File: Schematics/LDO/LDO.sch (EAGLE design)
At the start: 58 parts, among them IC1 LM317MBSTT3, IC2 LM317MBSTT3, Q1 32.768kHz, X1 MINI-USB-SHIELD-UX60-MB-5ST, X2 RJ45

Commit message: Layout Update
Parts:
- removed LED2: GREEN, led:LED5MM
- removed R2: 330, rcl:R-US_R0603
- removed U$4: SPST, Switches_SPST:SPST
- added H1, H2, H3, H4: MOUNT-HOLE3.0, holes:MOUNT-HOLE3.0
- ISP: device pinhead:PINHD-2X5/90 -> con-samtec:FTSH-105-01-L-DV-K
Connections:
- removed net N$12: LED2.C, R2.2
- removed net N$22: U$1.40
- removed net N$45: U$1.8, U$4.A1, U$4.A2
- new net PE: C13.1, R10.1, X1.GND1, X1.GND2, X1.GND3, X1.GND4
- net +3V3: now also C16.2, U$1.17, U$5.B1, U$5.B2, U$6.B1, U$6.B2
- net +5V: now also X2.4; no longer C16.2, U$1.17, X2.5
- net AGND: now also C14.1, C15.1, C3.1, C6.1, U$1.47, X2.3; no longer C13.1, R10.1, U$4.B1, U$4.B2, U$5.B1, U$5.B2, U$6.B1, U$6.B2, X1.GND1, X1.GND2, X1.GND3, X1.GND4
- net ANALOGINPUT: now also X2.7; no longer X2.2
- net GND: now also X1.4; no longer C14.1, C15.1, C3.1, C6.1, R2.1, U$1.47, X2.6
- net N$18: now also X2.5; no longer X2.3
- net N$19: now also X2.6; no longer X2.4
- net N$20: now also X2.2; no longer X2.7
- net N$21: now also X2.1; no longer X2.8
- net N$41: now also U$1.15; no longer U$1.9
- net N$42: now also X2.8; no longer X2.1
- net N$44: now also U$1.16; no longer U$1.11
- net V+: no longer LED2.A
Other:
- moved on the sheet: R13, X2

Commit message: LDO Layout
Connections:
- removed net AGND: C14.1, C15.1, C3.1, C6.1, U$1.47, X2.3
- net GND: now also C14.1, C15.1, C3.1, C6.1, U$1.47, X2.3
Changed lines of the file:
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@@
 <part name="+3V12" library="supply1" deviceset="+3V3" device=""/>
 <part name="GND4" library="supply1" deviceset="GND" device=""/>
-<part name="AGND6" library="supply1" deviceset="AGND" device=""/>
-<part name="AGND7" library="supply1" deviceset="AGND" device=""/>
-<part name="AGND8" library="supply1" deviceset="AGND" device=""/>
 <part name="PE1" library="supply1" deviceset="PE" device=""/>
-<part name="AGND1" library="supply1" deviceset="AGND" device=""/>
 <part name="GND6" library="supply1" deviceset="GND" device=""/>
 <part name="GND10" library="supply1" deviceset="GND" device=""/>
@@
 <part name="H3" library="holes" deviceset="MOUNT-HOLE" device="3.0"/>
 <part name="H4" library="holes" deviceset="MOUNT-HOLE" device="3.0"/>
+<part name="GND14" library="supply1" deviceset="GND" device=""/>
+<part name="GND15" library="supply1" deviceset="GND" device=""/>
+<part name="GND16" library="supply1" deviceset="GND" device=""/>
+<part name="GND21" library="supply1" deviceset="GND" device=""/>
 </parts>
 <sheets>
@@
 <instance part="+3V12" gate="G$1" x="-17.78" y="45.72"/>
 <instance part="GND4" gate="1" x="-22.86" y="58.42"/>
-<instance part="AGND6" gate="VR1" x="35.56" y="88.9"/>
-<instance part="AGND7" gate="VR1" x="63.5" y="81.28"/>
-<instance part="AGND8" gate="VR1" x="66.04" y="73.66"/>
 <instance part="PE1" gate="M" x="127" y="-15.24"/>
-<instance part="AGND1" gate="VR1" x="-17.78" y="71.12"/>
 <instance part="GND6" gate="1" x="-38.1" y="35.56"/>
 <instance part="GND10" gate="1" x="-45.72" y="35.56"/>
@@
 <instance part="H3" gate="G$1" x="48.26" y="-27.94"/>
 <instance part="H4" gate="G$1" x="58.42" y="-27.94"/>
+<instance part="GND14" gate="1" x="-17.78" y="71.12"/>
+<instance part="GND15" gate="1" x="35.56" y="88.9"/>
+<instance part="GND16" gate="1" x="66.04" y="73.66"/>
+<instance part="GND21" gate="1" x="63.5" y="81.28"/>
 </instances>
 <busses>
@@
 <pinref part="GND13" gate="1" pin="GND"/>
 </segment>
+<segment>
+<pinref part="C15" gate="G$1" pin="1"/>
+<pinref part="GND14" gate="1" pin="GND"/>
+</segment>
+<segment>
+<pinref part="C14" gate="G$1" pin="1"/>
+<wire x1="35.56" y1="91.44" x2="33.02" y2="91.44" width="0.1524" layer="91"/>
+<pinref part="X2" gate="G$1" pin="3"/>
+<wire x1="17.78" y1="111.76" x2="17.78" y2="93.98" width="0.1524" layer="91"/>
+<wire x1="17.78" y1="93.98" x2="33.02" y2="93.98" width="0.1524" layer="91"/>
+<wire x1="33.02" y1="93.98" x2="33.02" y2="91.44" width="0.1524" layer="91"/>
+<junction x="33.02" y="91.44"/>
+<pinref part="GND15" gate="1" pin="GND"/>
+</segment>
+<segment>
+<pinref part="U$1" gate="G$1" pin="47"/>
+<wire x1="45.72" y1="78.74" x2="66.04" y2="78.74" width="0.1524" layer="91"/>
+<wire x1="66.04" y1="78.74" x2="66.04" y2="76.2" width="0.1524" layer="91"/>
+<pinref part="C3" gate="G$1" pin="1"/>
+<wire x1="66.04" y1="76.2" x2="63.5" y2="76.2" width="0.1524" layer="91"/>
+<pinref part="GND16" gate="1" pin="GND"/>
+<junction x="66.04" y="76.2"/>
+</segment>
+<segment>
+<pinref part="C6" gate="G$1" pin="1"/>
+<pinref part="GND21" gate="1" pin="GND"/>
+</segment>
 </net>
 <net name="N$11" class="0">
@@
 </segment>
 </net>
-<net name="AGND" class="0">
-<segment>
-<pinref part="C14" gate="G$1" pin="1"/>
-<wire x1="35.56" y1="91.44" x2="33.02" y2="91.44" width="0.1524" layer="91"/>
-<pinref part="AGND6" gate="VR1" pin="AGND"/>
-<pinref part="X2" gate="G$1" pin="3"/>
-<wire x1="17.78" y1="111.76" x2="17.78" y2="93.98" width="0.1524" layer="91"/>
-<wire x1="17.78" y1="93.98" x2="33.02" y2="93.98" width="0.1524" layer="91"/>
-<wire x1="33.02" y1="93.98" x2="33.02" y2="91.44" width="0.1524" layer="91"/>
-<junction x="33.02" y="91.44"/>
-</segment>
-<segment>
-<pinref part="C6" gate="G$1" pin="1"/>
-<pinref part="AGND7" gate="VR1" pin="AGND"/>
-</segment>
-<segment>
-<pinref part="U$1" gate="G$1" pin="47"/>
-<wire x1="45.72" y1="78.74" x2="66.04" y2="78.74" width="0.1524" layer="91"/>
-<wire x1="66.04" y1="78.74" x2="66.04" y2="76.2" width="0.1524" layer="91"/>
-<pinref part="C3" gate="G$1" pin="1"/>
-<wire x1="66.04" y1="76.2" x2="63.5" y2="76.2" width="0.1524" layer="91"/>
-<pinref part="AGND8" gate="VR1" pin="AGND"/>
-<junction x="66.04" y="76.2"/>
-</segment>
-<segment>
-<pinref part="C15" gate="G$1" pin="1"/>
-<pinref part="AGND1" gate="VR1" pin="AGND"/>
-</segment>
-</net>

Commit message: Layout for final inspection
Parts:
- R9: value 380 -> 383
- renumbered U$2 to D6
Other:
- note added: "B1"
- note added: "B2"
- note added: "D10"
- note added: "RGB LED"
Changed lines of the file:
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@@
 <part name="D4" library="diode" deviceset="DIODE-" device="DO41-7.6" value="1N4002"/>
 <part name="R8" library="rcl" deviceset="R-US_" device="M1206" value="240"/>
-<part name="R9" library="rcl" deviceset="R-US_" device="M1206" value="380"/>
+<part name="R9" library="rcl" deviceset="R-US_" device="M1206" value="383"/>
 <part name="GND17" library="supply1" deviceset="GND" device=""/>
 <part name="GND18" library="supply1" deviceset="GND" device=""/>
@@
 <part name="U$5" library="Switches_SPST" deviceset="SPST" device=""/>
 <part name="U$6" library="Switches_SPST" deviceset="SPST" device=""/>
-<part name="U$2" library="RGB_LED" deviceset="RGB_LED" device=""/>
+<part name="D6" library="RGB_LED" deviceset="RGB_LED" device=""/>
 <part name="R16" library="rcl" deviceset="R-US_" device="R0603" value="180"/>
 <part name="R17" library="rcl" deviceset="R-US_" device="R0603" value="100"/>
@@
 <text x="213.36" y="-83.82" size="2.54" layer="94">2</text>
 <text x="134.62" y="-91.44" size="2.54" layer="94">4/28/2014</text>
+<text x="2.54" y="-35.56" size="1.778" layer="95">D10</text>
+<text x="2.54" y="-38.1" size="1.778" layer="95">RGB LED</text>
+<text x="-15.24" y="5.08" size="1.778" layer="95">B1</text>
+<text x="-15.24" y="-5.08" size="1.778" layer="95">B2</text>
 </plain>
 <instances>
 <instance part="U$1" gate="G$1" x="20.32" y="55.88"/>
-<instance part="X2" gate="G$1" x="20.32" y="116.84" rot="R90"/>
+<instance part="X2" gate="G$1" x="20.32" y="116.84" smashed="yes" rot="R90">
+<attribute name="NAME" x="15.24" y="121.92" size="1.778" layer="95" rot="R180"/>
+<attribute name="VALUE" x="33.528" y="111.76" size="1.778" layer="96" rot="R90"/>
+</instance>
 <instance part="ISP" gate="G$1" x="53.34" y="2.54"/>
 <instance part="POWER_IN" gate="G$1" x="-60.96" y="93.98"/>
@@
 <instance part="+3V7" gate="G$1" x="53.34" y="124.46"/>
 <instance part="R14" gate="G$1" x="7.62" y="114.3" smashed="yes" rot="R90">
-<attribute name="NAME" x="13.7414" y="115.57" size="1.778" layer="95" rot="R90"/>
-<attribute name="VALUE" x="10.922" y="113.03" size="1.778" layer="96" rot="R90"/>
+<attribute name="NAME" x="6.1214" y="107.95" size="1.778" layer="95" rot="R90"/>
+<attribute name="VALUE" x="10.922" y="115.57" size="1.778" layer="96" rot="R90"/>
 </instance>
 <instance part="R15" gate="G$1" x="0" y="114.3" smashed="yes" rot="R90">
@@
 <instance part="U$5" gate="G$1" x="-17.78" y="7.62"/>
 <instance part="U$6" gate="G$1" x="-17.78" y="-2.54"/>
-<instance part="U$2" gate="G$1" x="0" y="-35.56" rot="R180"/>
+<instance part="D6" gate="G$1" x="0" y="-35.56" rot="R180"/>
 <instance part="R16" gate="G$1" x="0" y="-15.24" smashed="yes" rot="R90">
 <attribute name="NAME" x="-1.4986" y="-19.05" size="1.778" layer="95" rot="R90"/>
@@
 </segment>
 <segment>
-<pinref part="U$2" gate="G$1" pin="VCC1"/>
+<pinref part="D6" gate="G$1" pin="VCC1"/>
 <wire x1="0" y1="-40.64" x2="-17.78" y2="-40.64" width="0.1524" layer="91"/>
 <wire x1="-17.78" y1="-40.64" x2="-17.78" y2="-17.78" width="0.1524" layer="91"/>
@@
 <net name="N$24" class="0">
 <segment>
-<pinref part="U$2" gate="G$1" pin="G4"/>
+<pinref part="D6" gate="G$1" pin="G4"/>
 <pinref part="R17" gate="G$1" pin="1"/>
 </segment>
@@
 <net name="N$25" class="0">
 <segment>
-<pinref part="U$2" gate="G$1" pin="R3"/>
+<pinref part="D6" gate="G$1" pin="R3"/>
 <pinref part="R16" gate="G$1" pin="1"/>
 <wire x1="0" y1="-22.86" x2="0" y2="-20.32" width="0.1524" layer="91"/>
@@
 <net name="N$26" class="0">
 <segment>
-<pinref part="U$2" gate="G$1" pin="B2"/>
+<pinref part="D6" gate="G$1" pin="B2"/>
 <pinref part="R18" gate="G$1" pin="1"/>
 <wire x1="7.62" y1="-22.86" x2="7.62" y2="-20.32" width="0.1524" layer="91"/>

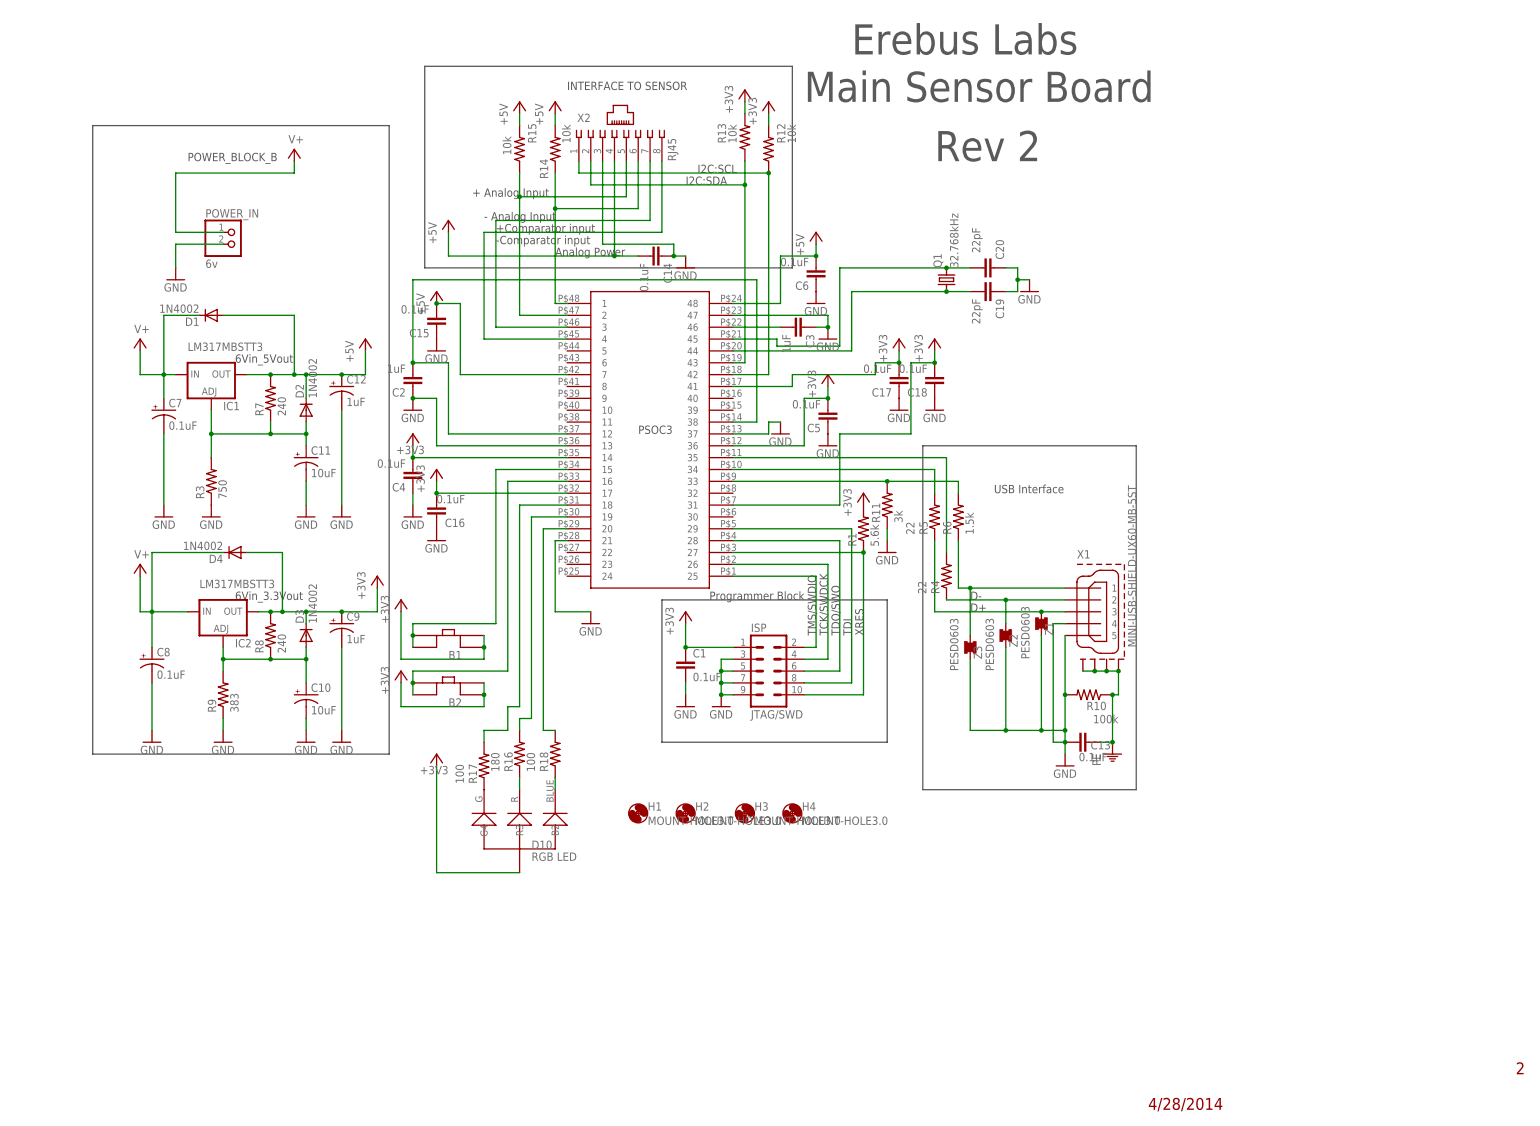
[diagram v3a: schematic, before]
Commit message: Added Battery Sense to LDO
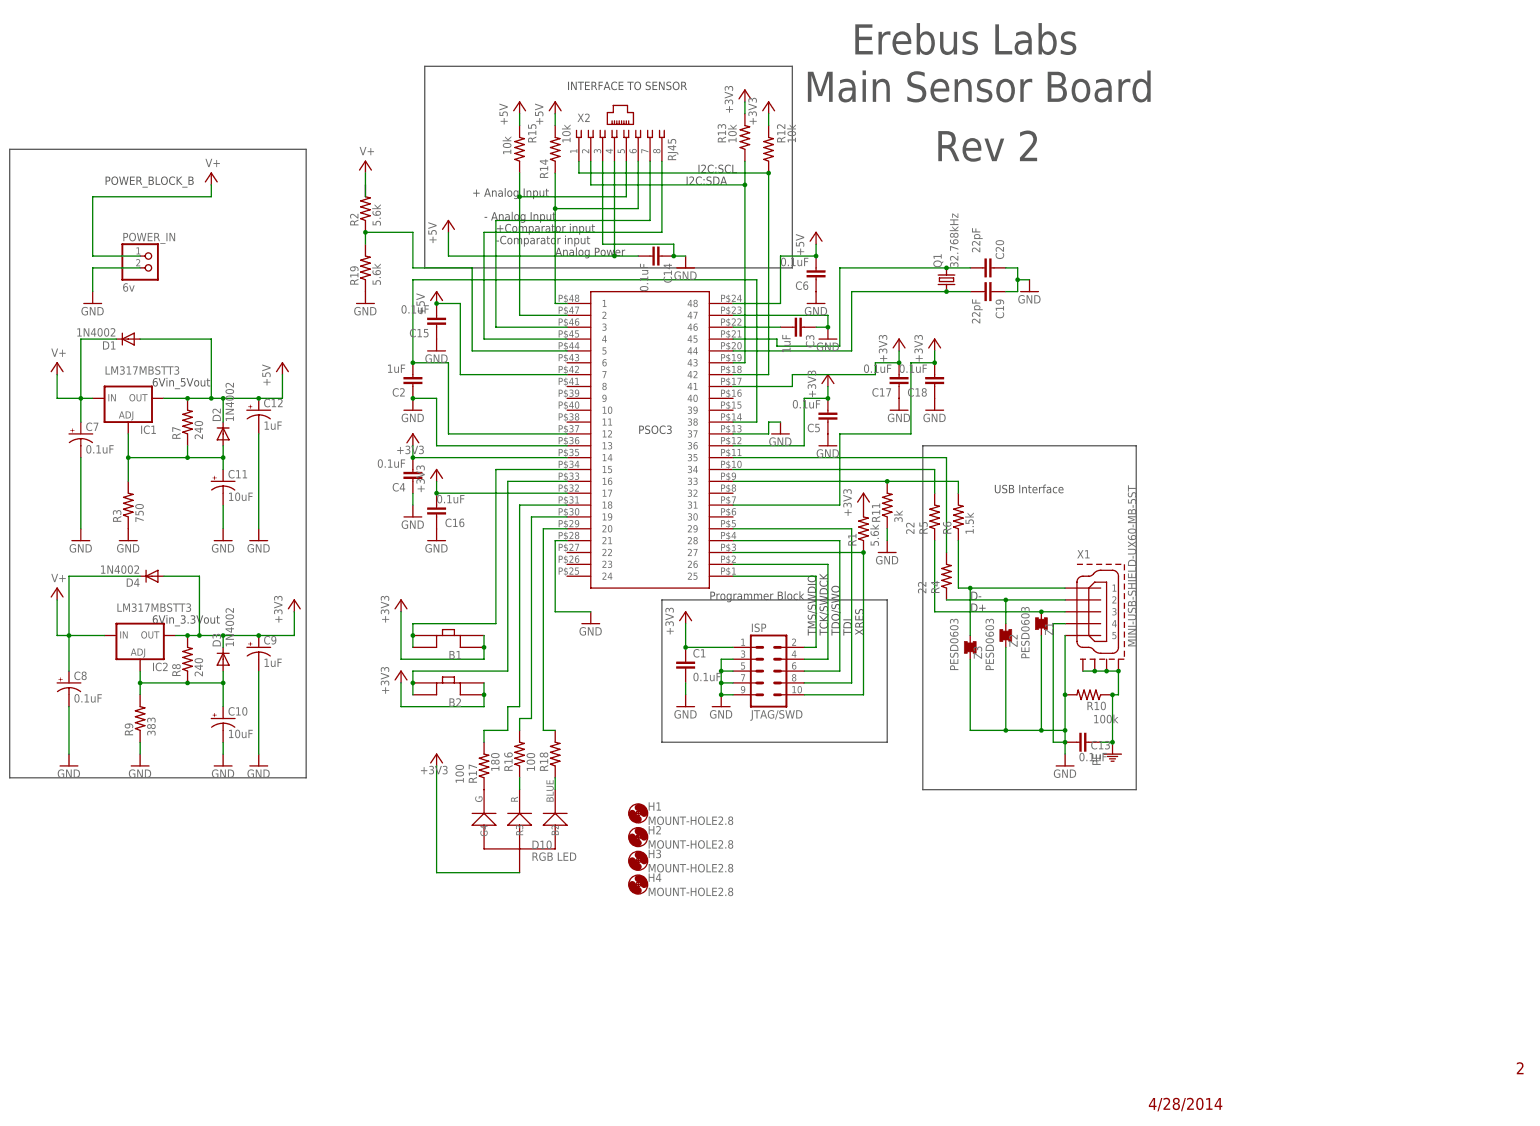
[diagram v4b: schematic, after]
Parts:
- added R19, R2: 5.6k, rcl:R-US_R0805
- H1, H2, H3, H4: value MOUNT-HOLE3.0 -> MOUNT-HOLE2.8; device holes:MOUNT-HOLE3.0 -> holes:MOUNT-HOLE2.8
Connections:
- new net N$12: R19.2, R2.1, U$1.5
- net GND: now also R19.1
- net V+: now also R2.2
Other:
- moved on the sheet: C10, C11, C12, C7, C8, C9, D1, D2, D3, D4, H2, H3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

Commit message: Cleaned up stuff
Made Schematics easier to read
Split Supplies in BOM and made names match references
Renamed parts on sensor
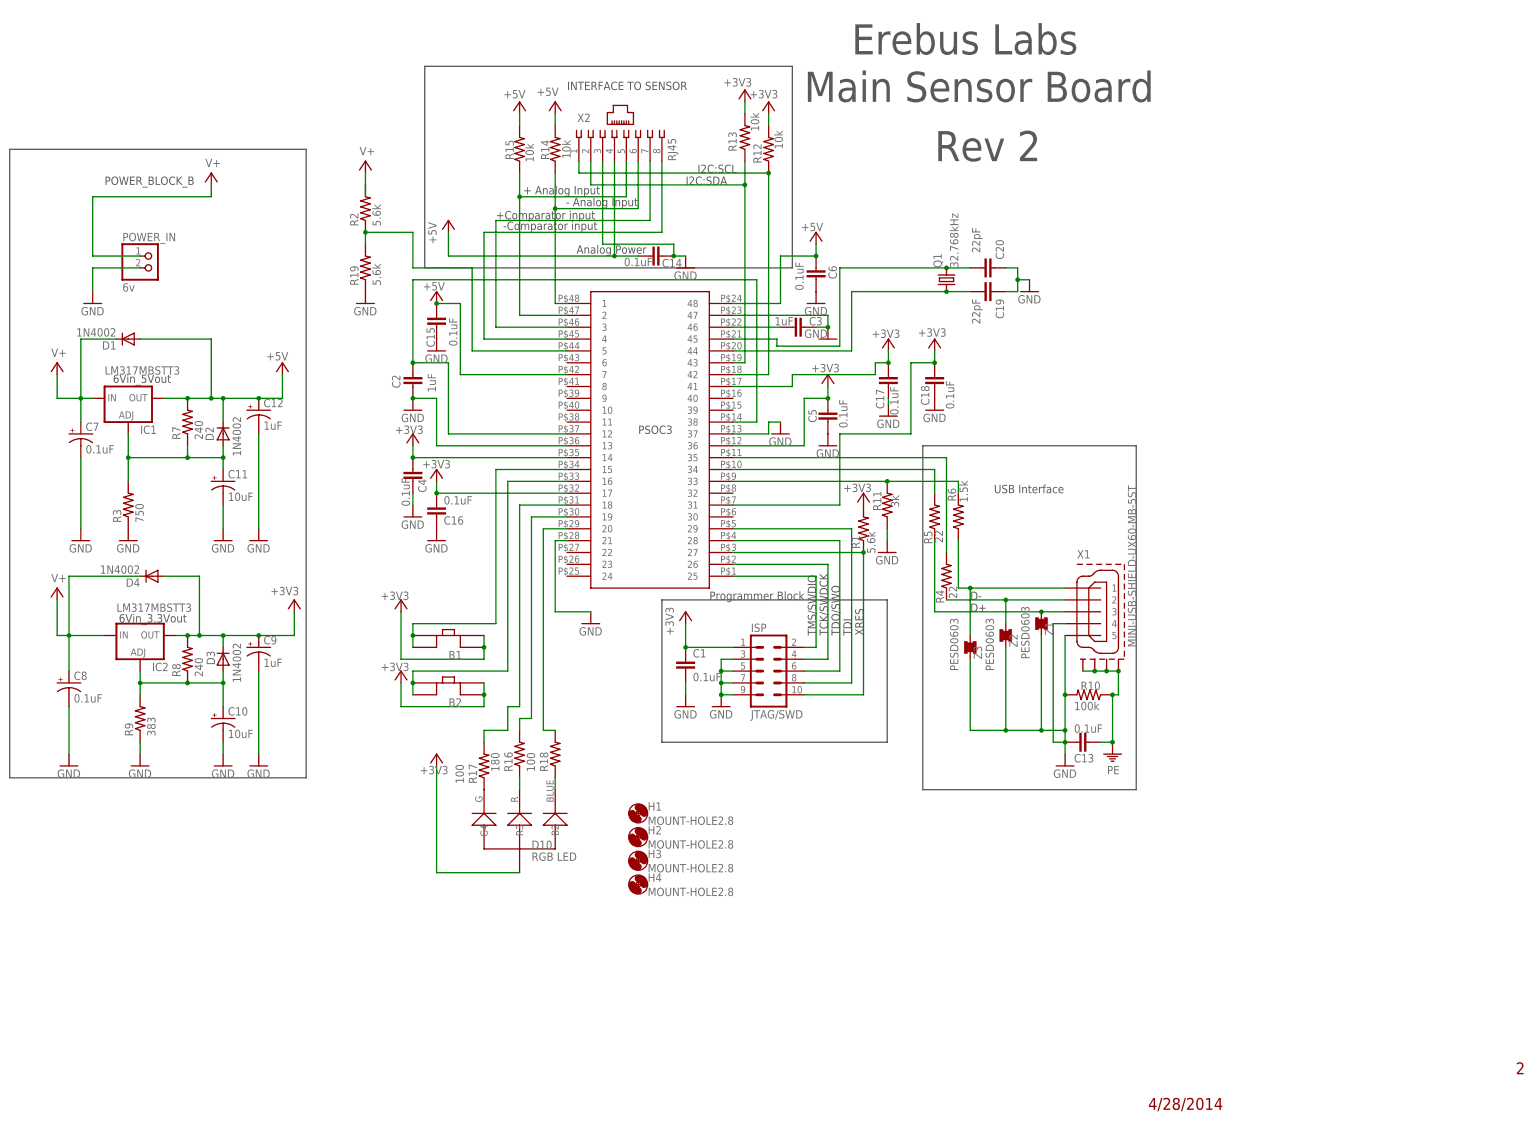
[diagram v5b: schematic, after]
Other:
- moved on the sheet: C17
